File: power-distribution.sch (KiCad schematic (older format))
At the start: 4 parts, among them CON1 2PIN_SCREWTERMINAL, CON2 2PIN_SCREWTERMINAL, CON3 2PIN_SCREWTERMINAL, CON4 2PIN_SCREWTERMINAL

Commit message: Added mounting holes and two more connectors
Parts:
- added CON5, CON6: 2PIN_SCREWTERMINAL, Pyth_Connectors:2PIN_Screw_Block, symbol 2PIN_SCREWTERMINAL
- added M? (x4): Mounting_hole, symbol Mounting_hole
- CON1, CON2, CON3, CON4: footprint (none) -> Pyth_Connectors:2PIN_Screw_Block
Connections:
- net at CON1.1, CON2.1, CON3.1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: now also CON5.1, CON6.1
- net at CON1.2, CON2.2, CON3.2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: now also CON5.2, CON6.2
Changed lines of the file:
@@
 LIBS:valves
 LIBS:pyth
+LIBS:power-distribution-cache
 EELAYER 24 0
 EELAYER END
@@
 F 0 "CON1" H 3350 2850 60  0000 C CNN
 F 1 "2PIN_SCREWTERMINAL" V 3050 3350 60  0000 C CNN
-F 2 "" H 3550 3300 60  0000 C CNN
+F 2 "Pyth_Connectors:2PIN_Screw_Block" H 3550 3300 60  0001 C CNN
 F 3 "" H 3550 3300 60  0000 C CNN
 	1    3550 3300
@@
 F 0 "CON2" H 3350 3900 60  0000 C CNN
 F 1 "2PIN_SCREWTERMINAL" V 3050 4400 60  0000 C CNN
-F 2 "" H 3550 4350 60  0000 C CNN
+F 2 "Pyth_Connectors:2PIN_Screw_Block" H 3550 4350 60  0001 C CNN
 F 3 "" H 3550 4350 60  0000 C CNN
 	1    3550 4350
@@
 F 0 "CON3" H 3350 4950 60  0000 C CNN
 F 1 "2PIN_SCREWTERMINAL" V 3050 5450 60  0000 C CNN
-F 2 "" H 3550 5400 60  0000 C CNN
+F 2 "Pyth_Connectors:2PIN_Screw_Block" H 3550 5400 60  0001 C CNN
 F 3 "" H 3550 5400 60  0000 C CNN
 	1    3550 5400
@@
 F 0 "CON4" H 3350 5950 60  0000 C CNN
 F 1 "2PIN_SCREWTERMINAL" V 3050 6450 60  0000 C CNN
-F 2 "" H 3550 6400 60  0000 C CNN
+F 2 "Pyth_Connectors:2PIN_Screw_Block" H 3550 6400 60  0001 C CNN
 F 3 "" H 3550 6400 60  0000 C CNN
 	1    3550 6400
@@
 	3650 5600 4200 5600
 Connection ~ 4200 5600
+$Comp
+L 2PIN_SCREWTERMINAL CON5
+U 1 1 5416EE7E
+P 4750 4100
+F 0 "CON5" H 4550 3650 60  0000 C CNN
+F 1 "2PIN_SCREWTERMINAL" V 4250 4150 60  0000 C CNN
+F 2 "Pyth_Connectors:2PIN_Screw_Block" H 4750 4100 60  0001 C CNN
+F 3 "" H 4750 4100 60  0000 C CNN
+	1    4750 4100
+	-1   0    0    1
+$EndComp
+$Comp
+L 2PIN_SCREWTERMINAL CON6
+U 1 1 5416EF02
+P 4750 5100
+F 0 "CON6" H 4550 4650 60  0000 C CNN
+F 1 "2PIN_SCREWTERMINAL" V 4250 5150 60  0000 C CNN
+F 2 "Pyth_Connectors:2PIN_Screw_Block" H 4750 5100 60  0001 C CNN
+F 3 "" H 4750 5100 60  0000 C CNN
+	1    4750 5100
+	-1   0    0    1
+$EndComp
+Wire Wire Line
+	4650 5400 3950 5400
+Connection ~ 3950 5400
+Wire Wire Line
+	4650 4900 4200 4900
+Connection ~ 4200 4900
+Wire Wire Line
+	4650 3900 4200 3900
+Connection ~ 4200 3900
+Wire Wire Line
+	4650 4400 3950 4400
+Connection ~ 3950 4400
+$Comp
+L Mounting_hole M?
+U 1 1 5416F0DF
+P 4550 2050
+F 0 "M?" H 4550 1750 60  0000 C CNN
+F 1 "Mounting_hole" H 4550 2250 60  0000 C CNN
+F 2 "" H 4550 2050 60  0000 C CNN
+F 3 "" H 4550 2050 60  0000 C CNN
+	1    4550 2050
+	1    0    0    -1
+$EndComp
+$Comp
+L Mounting_hole M?
+U 1 1 5416F10E
+P 5250 2050
+F 0 "M?" H 5250 1750 60  0000 C CNN
+F 1 "Mounting_hole" H 5250 2250 60  0000 C CNN
+F 2 "" H 5250 2050 60  0000 C CNN
+F 3 "" H 5250 2050 60  0000 C CNN
+	1    5250 2050
+	1    0    0    -1
+$EndComp
+$Comp
+L Mounting_hole M?
+U 1 1 5416F227
+P 5950 2050
+F 0 "M?" H 5950 1750 60  0000 C CNN
+F 1 "Mounting_hole" H 5950 2250 60  0000 C CNN
+F 2 "" H 5950 2050 60  0000 C CNN
+F 3 "" H 5950 2050 60  0000 C CNN
+	1    5950 2050
+	1    0    0    -1
+$EndComp
+$Comp
+L Mounting_hole M?
+U 1 1 5416F260
+P 6650 2050
+F 0 "M?" H 6650 1750 60  0000 C CNN
+F 1 "Mounting_hole" H 6650 2250 60  0000 C CNN
+F 2 "" H 6650 2050 60  0000 C CNN
+F 3 "" H 6650 2050 60  0000 C CNN
+	1    6650 2050
+	1    0    0    -1
+$EndComp
 $EndSCHEMATC

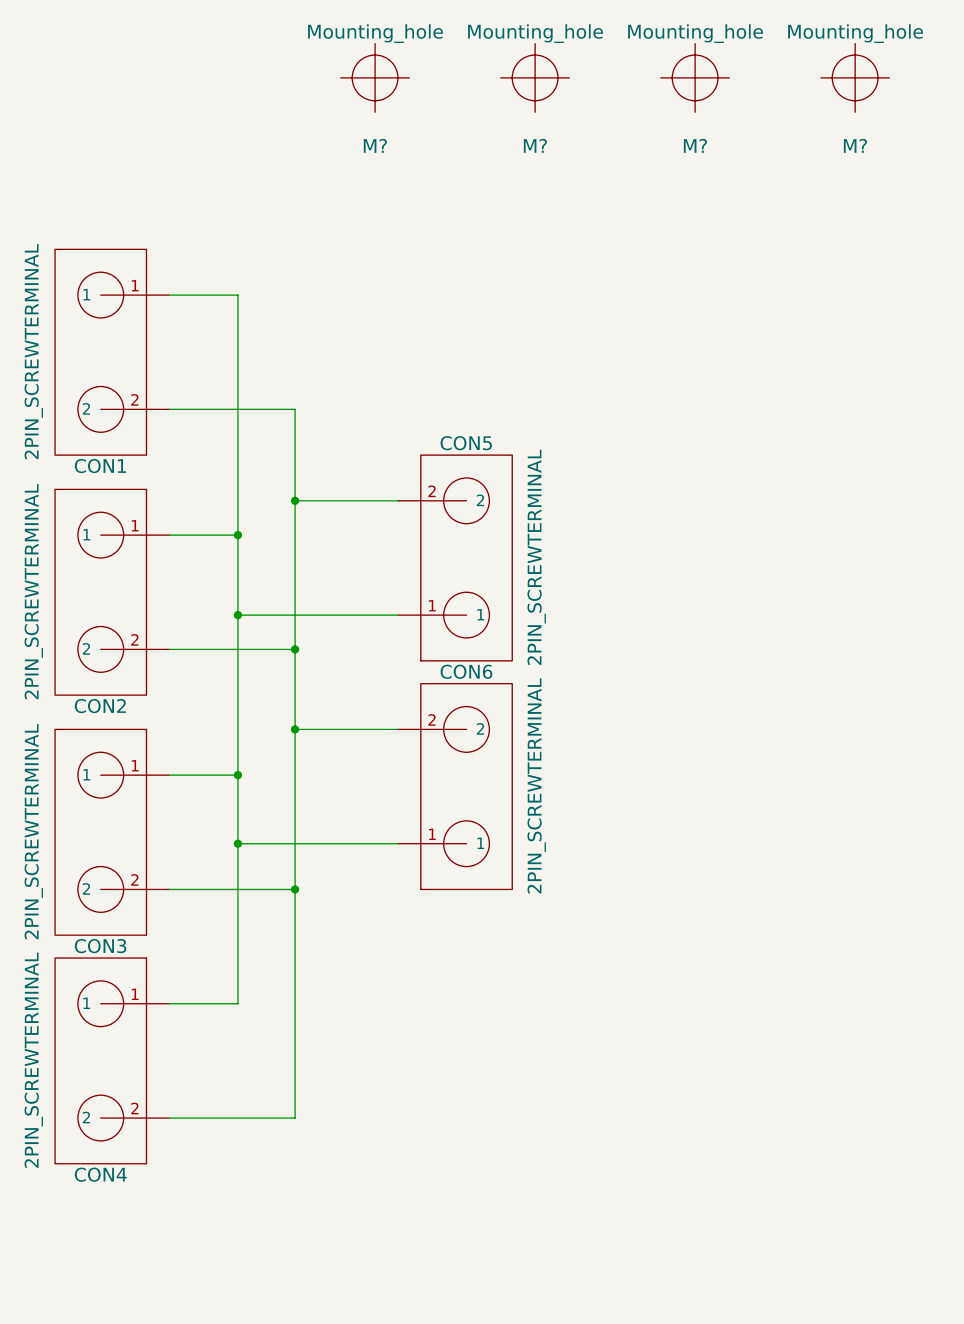
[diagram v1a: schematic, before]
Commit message: Split into two power planes, with jumpers in the middle to connect
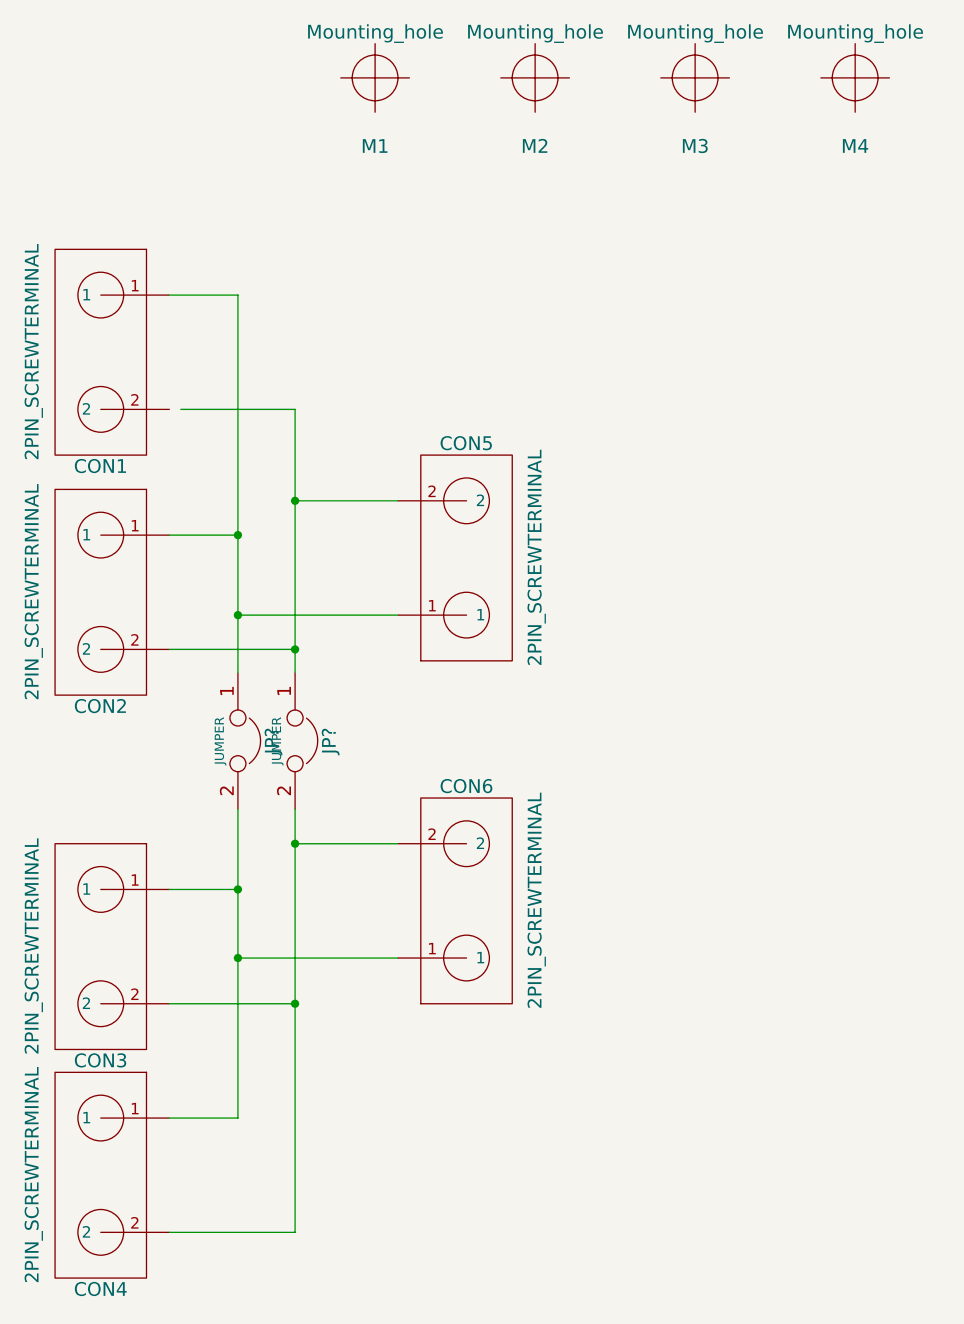
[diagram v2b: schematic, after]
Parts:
- added JP? (x2): JUMPER, symbol JUMPER
- M1, M2, M3, M4: renamed from M?; footprint (none) -> Mounting_Holes:MountingHole_3mm
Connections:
- wire segments 14 -> 16
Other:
- moved on the sheet: CON3, CON4, CON6
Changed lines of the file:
@@
 L 2PIN_SCREWTERMINAL CON3
 U 1 1 5411B882
-P 3550 5400
-F 0 "CON3" H 3350 4950 60  0000 C CNN
-F 1 "2PIN_SCREWTERMINAL" V 3050 5450 60  0000 C CNN
-F 2 "Pyth_Connectors:2PIN_Screw_Block" H 3550 5400 60  0001 C CNN
-F 3 "" H 3550 5400 60  0000 C CNN
-	1    3550 5400
+P 3550 5900
+F 0 "CON3" H 3350 5450 60  0000 C CNN
+F 1 "2PIN_SCREWTERMINAL" V 3050 5950 60  0000 C CNN
+F 2 "Pyth_Connectors:2PIN_Screw_Block" H 3550 5900 60  0001 C CNN
+F 3 "" H 3550 5900 60  0000 C CNN
+	1    3550 5900
 	1    0    0    -1
 $EndComp
@@
 L 2PIN_SCREWTERMINAL CON4
 U 1 1 5411B896
-P 3550 6400
-F 0 "CON4" H 3350 5950 60  0000 C CNN
-F 1 "2PIN_SCREWTERMINAL" V 3050 6450 60  0000 C CNN
-F 2 "Pyth_Connectors:2PIN_Screw_Block" H 3550 6400 60  0001 C CNN
-F 3 "" H 3550 6400 60  0000 C CNN
-	1    3550 6400
+P 3550 6900
+F 0 "CON4" H 3350 6450 60  0000 C CNN
+F 1 "2PIN_SCREWTERMINAL" V 3050 6950 60  0000 C CNN
+F 2 "Pyth_Connectors:2PIN_Screw_Block" H 3550 6900 60  0001 C CNN
+F 3 "" H 3550 6900 60  0000 C CNN
+	1    3550 6900
 	1    0    0    -1
 $EndComp
 Wire Wire Line
-	3650 6100 3950 6100
-Wire Wire Line
-	3950 6100 3950 3000
-Wire Wire Line
-	3950 3000 3650 3000
+	3950 6600 3650 6600
 Wire Wire Line
 	3650 4050 3950 4050
 Connection ~ 3950 4050
 Wire Wire Line
-	3650 5100 3950 5100
-Connection ~ 3950 5100
+	3650 5600 3950 5600
+Connection ~ 3950 5600
 Wire Wire Line
-	3650 6600 4200 6600
-Wire Wire Line
-	4200 6600 4200 3500
-Wire Wire Line
-	4200 3500 3650 3500
+	4200 7100 3650 7100
 Wire Wire Line
 	3650 4550 4200 4550
 Connection ~ 4200 4550
 Wire Wire Line
-	3650 5600 4200 5600
-Connection ~ 4200 5600
+	3650 6100 4200 6100
+Connection ~ 4200 6100
 $Comp
 L 2PIN_SCREWTERMINAL CON5
@@
 L 2PIN_SCREWTERMINAL CON6
 U 1 1 5416EF02
-P 4750 5100
-F 0 "CON6" H 4550 4650 60  0000 C CNN
-F 1 "2PIN_SCREWTERMINAL" V 4250 5150 60  0000 C CNN
-F 2 "Pyth_Connectors:2PIN_Screw_Block" H 4750 5100 60  0001 C CNN
-F 3 "" H 4750 5100 60  0000 C CNN
-	1    4750 5100
+P 4750 5600
+F 0 "CON6" H 4550 5150 60  0000 C CNN
+F 1 "2PIN_SCREWTERMINAL" V 4250 5650 60  0000 C CNN
+F 2 "Pyth_Connectors:2PIN_Screw_Block" H 4750 5600 60  0001 C CNN
+F 3 "" H 4750 5600 60  0000 C CNN
+	1    4750 5600
 	-1   0    0    1
 $EndComp
 Wire Wire Line
-	4650 5400 3950 5400
-Connection ~ 3950 5400
+	4650 5900 3950 5900
+Connection ~ 3950 5900
 Wire Wire Line
-	4650 4900 4200 4900
-Connection ~ 4200 4900
+	4650 5400 4200 5400
+Connection ~ 4200 5400
 Wire Wire Line
 	4650 3900 4200 3900
@@
 Connection ~ 3950 4400
 $Comp
-L Mounting_hole M?
+L Mounting_hole M1
 U 1 1 5416F0DF
 P 4550 2050
-F 0 "M?" H 4550 1750 60  0000 C CNN
+F 0 "M1" H 4550 1750 60  0000 C CNN
 F 1 "Mounting_hole" H 4550 2250 60  0000 C CNN
-F 2 "" H 4550 2050 60  0000 C CNN
+F 2 "Mounting_Holes:MountingHole_3mm" H 4550 2050 60  0001 C CNN
 F 3 "" H 4550 2050 60  0000 C CNN
 	1    4550 2050
@@
 $EndComp
 $Comp
-L Mounting_hole M?
+L Mounting_hole M2
 U 1 1 5416F10E
 P 5250 2050
-F 0 "M?" H 5250 1750 60  0000 C CNN
+F 0 "M2" H 5250 1750 60  0000 C CNN
 F 1 "Mounting_hole" H 5250 2250 60  0000 C CNN
-F 2 "" H 5250 2050 60  0000 C CNN
+F 2 "Mounting_Holes:MountingHole_3mm" H 5250 2050 60  0001 C CNN
 F 3 "" H 5250 2050 60  0000 C CNN
 	1    5250 2050
@@
 $EndComp
 $Comp
-L Mounting_hole M?
+L Mounting_hole M3
 U 1 1 5416F227
 P 5950 2050
-F 0 "M?" H 5950 1750 60  0000 C CNN
+F 0 "M3" H 5950 1750 60  0000 C CNN
 F 1 "Mounting_hole" H 5950 2250 60  0000 C CNN
-F 2 "" H 5950 2050 60  0000 C CNN
+F 2 "Mounting_Holes:MountingHole_3mm" H 5950 2050 60  0001 C CNN
 F 3 "" H 5950 2050 60  0000 C CNN
 	1    5950 2050
@@
 $EndComp
 $Comp
-L Mounting_hole M?
+L Mounting_hole M4
 U 1 1 5416F260
 P 6650 2050
-F 0 "M?" H 6650 1750 60  0000 C CNN
+F 0 "M4" H 6650 1750 60  0000 C CNN
 F 1 "Mounting_hole" H 6650 2250 60  0000 C CNN
-F 2 "" H 6650 2050 60  0000 C CNN
+F 2 "Mounting_Holes:MountingHole_3mm" H 6650 2050 60  0001 C CNN
 F 3 "" H 6650 2050 60  0000 C CNN
 	1    6650 2050
 	1    0    0    -1
 $EndComp
+Wire Wire Line
+	3950 3000 3950 4650
+Wire Wire Line
+	3950 3000 3650 3000
+Wire Wire Line
+	3700 3500 4200 3500
+Wire Wire Line
+	4200 3500 4200 4650
+Wire Wire Line
+	4200 5250 4200 7100
+Wire Wire Line
+	3950 5250 3950 6600
+$Comp
+L JUMPER JP?
+U 1 1 5416F67E
+P 3950 4950
+F 0 "JP?" H 3950 5100 60  0000 C CNN
+F 1 "JUMPER" H 3950 4870 40  0000 C CNN
+F 2 "" H 3950 4950 60  0000 C CNN
+F 3 "" H 3950 4950 60  0000 C CNN
+	1    3950 4950
+	0    1    1    0
+$EndComp
+$Comp
+L JUMPER JP?
+U 1 1 5416F6C7
+P 4200 4950
+F 0 "JP?" H 4200 5100 60  0000 C CNN
+F 1 "JUMPER" H 4200 4870 40  0000 C CNN
+F 2 "" H 4200 4950 60  0000 C CNN
+F 3 "" H 4200 4950 60  0000 C CNN
+	1    4200 4950
+	0    1    1    0
+$EndComp
 $EndSCHEMATC
